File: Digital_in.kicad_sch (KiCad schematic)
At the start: 52 parts

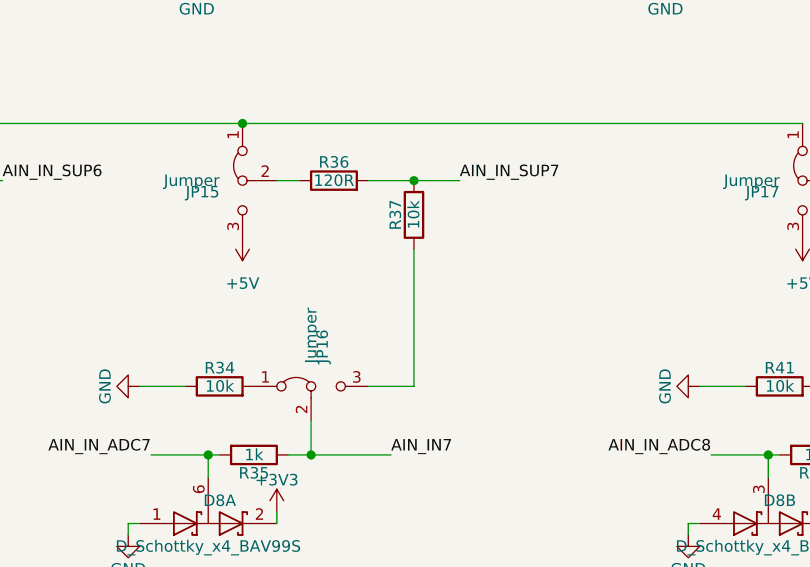
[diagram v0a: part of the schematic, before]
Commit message: UPDATE - LAN chipset waiting for verification
Signed-off-by: Jacek <matuszewski.kartech@gmail.com>
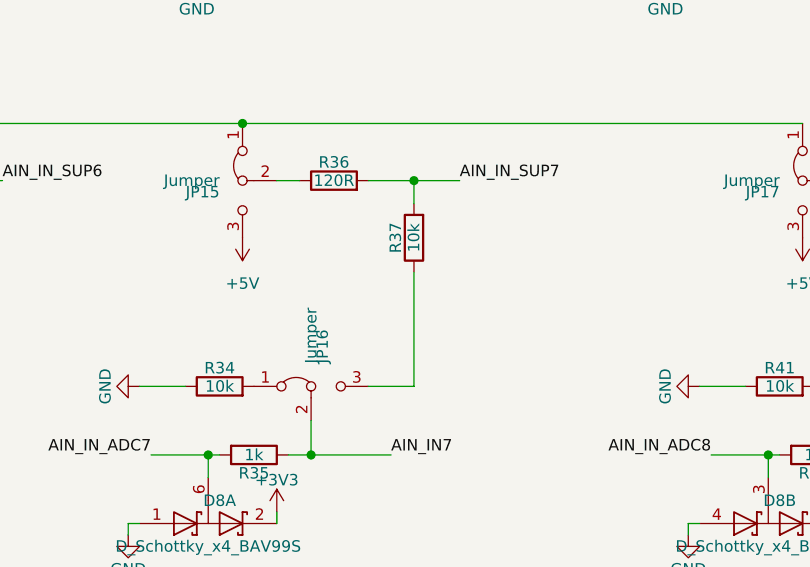
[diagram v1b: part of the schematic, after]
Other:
- moved on the sheet: R37
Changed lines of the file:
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@@
 (kicad_sch (version 20201015) (generator eeschema)
-  (page 1 12)
   (paper "A4")
   (title_block
@@
     (stroke (width 0) (type solid) (color 0 0 0 0))
   )
+  (wire (pts (xy 200.66 104.14) (xy 200.66 106.68))
+    (stroke (width 0) (type solid) (color 0 0 0 0))
+  )
   (wire (pts (xy 200.66 104.14) (xy 205.74 104.14))
     (stroke (width 0) (type solid) (color 0 0 0 0))
   )
-  (wire (pts (xy 200.66 127) (xy 200.66 111.76))
+  (wire (pts (xy 200.66 114.3) (xy 200.66 127))
     (stroke (width 0) (type solid) (color 0 0 0 0))
   )
@@
     )
   )
-  (symbol (lib_id "Uni_Printer-rescue:R-Sensor_tank_v1-rescue-Uni_General_v1-rescue-Uni_Printer_v1-rescue") (at 200.66 107.95 180) (unit 1)
-    (in_bom yes) (on_board yes)
-    (property "Reference" "R37" (id 0) (at 198.628 107.95 90))
-    (property "Value" "10k" (id 1) (at 200.66 107.95 90))
-    (property "Footprint" "Resistor_SMD:R_0603_1608Metric" (id 2) (at 202.438 107.95 90)
-      (effects (font (size 1.27 1.27)) hide)
-    )
-    (property "Datasheet" "" (id 3) (at 200.66 107.95 0)
-      (effects (font (size 1.27 1.27)) hide)
-    )
-    (property "TME" "SMD0603-680R-1%" (id 4) (at 200.66 107.95 90)
-      (effects (font (size 1.27 1.27)) hide)
-    )
+  (symbol (lib_id "Uni_Printer-rescue:R-Sensor_tank_v1-rescue-Uni_General_v1-rescue-Uni_Printer_v1-rescue") (at 200.66 110.49 180) (unit 1)
+    (in_bom yes) (on_board yes)
+    (property "Reference" "R37" (id 0) (at 198.628 110.49 90))
+    (property "Value" "10k" (id 1) (at 200.66 110.49 90))
+    (property "Footprint" "Resistor_SMD:R_0603_1608Metric" (id 2) (at 202.438 110.49 90)
+      (effects (font (size 1.27 1.27)) hide)
+    )
+    (property "Datasheet" "" (id 3) (at 200.66 110.49 0)
+      (effects (font (size 1.27 1.27)) hide)
+    )
+    (property "TME" "SMD0603-680R-1%" (id 4) (at 200.66 110.49 90)
+      (effects (font (size 1.27 1.27)) hide)
+    )

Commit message: UPDATE
Signed-off-by: Jacek <matuszewski.kartech@gmail.com>
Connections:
- net IN4: now also JP4.2 (C), R21.1
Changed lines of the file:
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@@
   (junction (at 237.49 71.12) (diameter 1.016) (color 0 0 0 0))
   (junction (at 240.03 134.62) (diameter 1.016) (color 0 0 0 0))
+  (junction (at 251.46 70.104) (diameter 1.016) (color 0 0 0 0))
   (junction (at 251.46 71.12) (diameter 1.016) (color 0 0 0 0))
   (junction (at 251.46 134.62) (diameter 1.016) (color 0 0 0 0))
+  (junction (at 255.524 63.5) (diameter 1.016) (color 0 0 0 0))
   (junction (at 260.35 40.64) (diameter 1.016) (color 0 0 0 0))
   (junction (at 262.89 104.14) (diameter 1.016) (color 0 0 0 0))
@@
     (stroke (width 0) (type solid) (color 0 0 0 0))
   )
-  (wire (pts (xy 251.46 69.85) (xy 251.46 71.12))
+  (wire (pts (xy 251.46 69.85) (xy 251.46 70.104))
+    (stroke (width 0) (type solid) (color 0 0 0 0))
+  )
+  (wire (pts (xy 251.46 70.104) (xy 251.46 71.12))
+    (stroke (width 0) (type solid) (color 0 0 0 0))
+  )
+  (wire (pts (xy 251.46 70.104) (xy 255.524 70.104))
     (stroke (width 0) (type solid) (color 0 0 0 0))
   )
@@
     (stroke (width 0) (type solid) (color 0 0 0 0))
   )
-  (wire (pts (xy 255.27 63.5) (xy 260.35 63.5))
-    (stroke (width 0) (type solid) (color 0 0 0 0))
-  )
+  (wire (pts (xy 255.27 63.5) (xy 255.524 63.5))
+    (stroke (width 0) (type solid) (color 0 0 0 0))
+  )
+  (wire (pts (xy 255.524 63.5) (xy 260.35 63.5))
+    (stroke (width 0) (type solid) (color 0 0 0 0))
+  )
+  (wire (pts (xy 255.524 70.104) (xy 255.524 63.5))
+    (stroke (width 0) (type solid) (color 0 0 0 0))
+  )

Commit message: Fixes
Signed-off-by: Jarosław Karwik <jaroslaw.karwik@gmail.com>
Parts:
- JP1, JP10, JP11, JP12, JP13, JP14, JP15, JP16, JP17, JP18, JP2, JP3, JP4, JP7, JP8, JP9: footprint Jumper:SolderJumper-3_P1.3mm_Bridged2Bar12_RoundedPad1.0x1.5mm -> moje:SolderJumper-3-open; TME WF06P-120R-5% -> (none)
- R10, R11, R12, R13, R14, R15, R16, R17, R18, R19, R20, R21: TME WF06P-120R-5% -> (none)
- R26, R29, R30, R33, R34, R37, R41, R44, R7, R9: TME SMD0603-680R-1% -> (none)
- R27, R31, R35, R42, R6: TME HP03-1K5% -> (none)
- R28, R32, R36, R43, R8: TME CRCW06030000Z0TABC -> (none)
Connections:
- net IN4: no longer JP4.2 (C), R21.1
- new net: JP4.2 (C), R21.1

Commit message: UPDATE - 3D and Jumper descriptions
Signed-off-by: Jacek <matuszewski.kartech@gmail.com>
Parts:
- JP1: value Jumper -> IN1_P
- JP10: value Jumper -> IN4
- JP11: value Jumper -> IN5
- JP12: value Jumper -> IN5_P
- JP13: value Jumper -> IN6
- JP14: value Jumper -> IN6_P
- JP15: value Jumper -> IN7
- JP16: value Jumper -> IN7_P
- JP17: value Jumper -> IN8
- JP18: value Jumper -> IN8_P
- JP2: value Jumper -> IN2_P
- JP3: value Jumper -> IN3_P
- JP4: value Jumper -> IN4_P
- JP7: value Jumper -> IN1
- JP8: value Jumper -> IN2
- JP9: value Jumper -> IN3
- R10, R14, R18, R27, R31, R35, R42, R6: TME (none) -> SMD0603-1K
- R11, R13, R15, R17, R19, R21, R26, R29, R30, R33, R34, R37, R41, R44, R7, R9: TME (none) -> SMD0603-10K
- R12, R16, R20, R28, R32, R36, R43, R8: TME (none) -> WF06P-120R-5%
